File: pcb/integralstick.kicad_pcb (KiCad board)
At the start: 4 copper layers, 219 parts, among them J1 CONN_INTEGRALSTICK_FPGA_DEVICE, J2 CONN_INTEGRALSTICK_MCU_DEVICE, Q1 SSM6N58NU, Q2 SSM6N58NU, Q3 SSM6N58NU, U1 STM32F777NIH6‎, U10 DSC6083MI2A-032K768, U12 DSC6001HI2A-025.0000‎, U2 XC7A50T-1FTG256C, U3 S27KS0641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

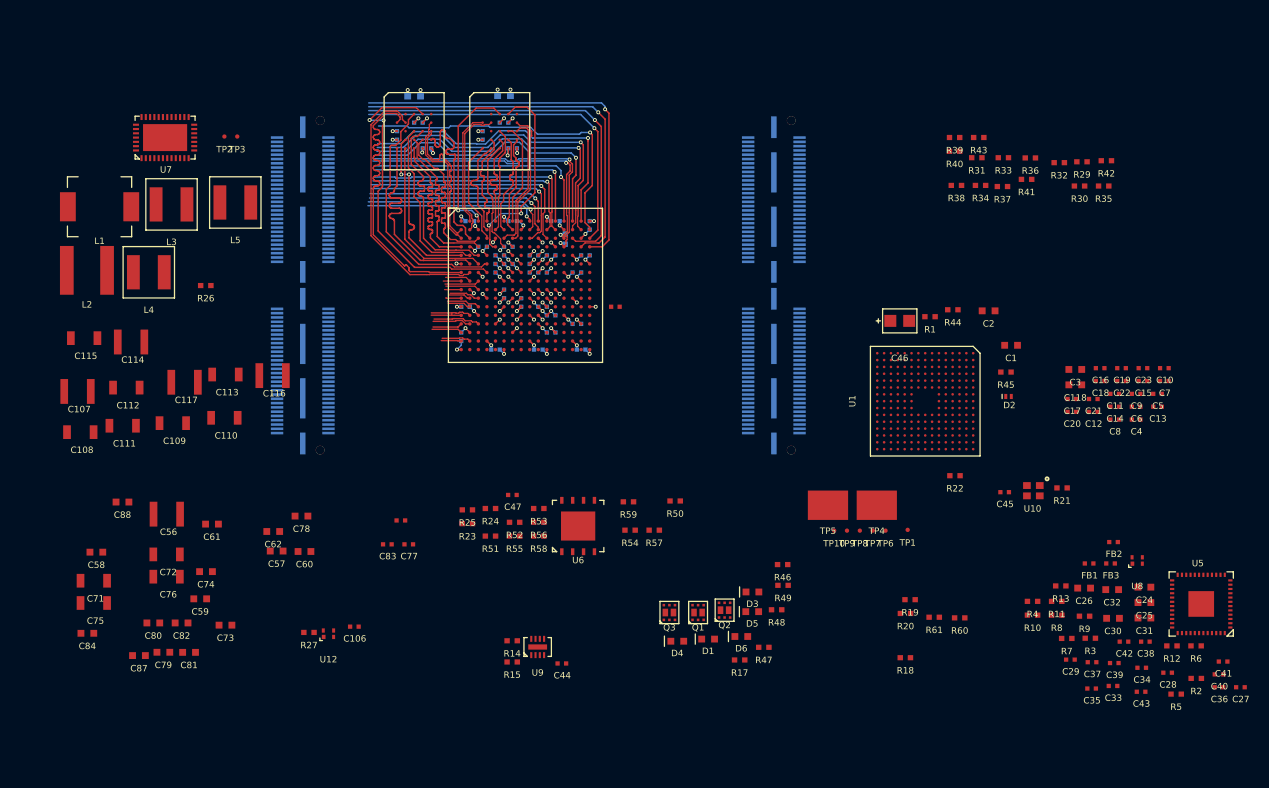
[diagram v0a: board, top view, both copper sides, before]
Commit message: Lots more routing of 3.3V GPIO bus
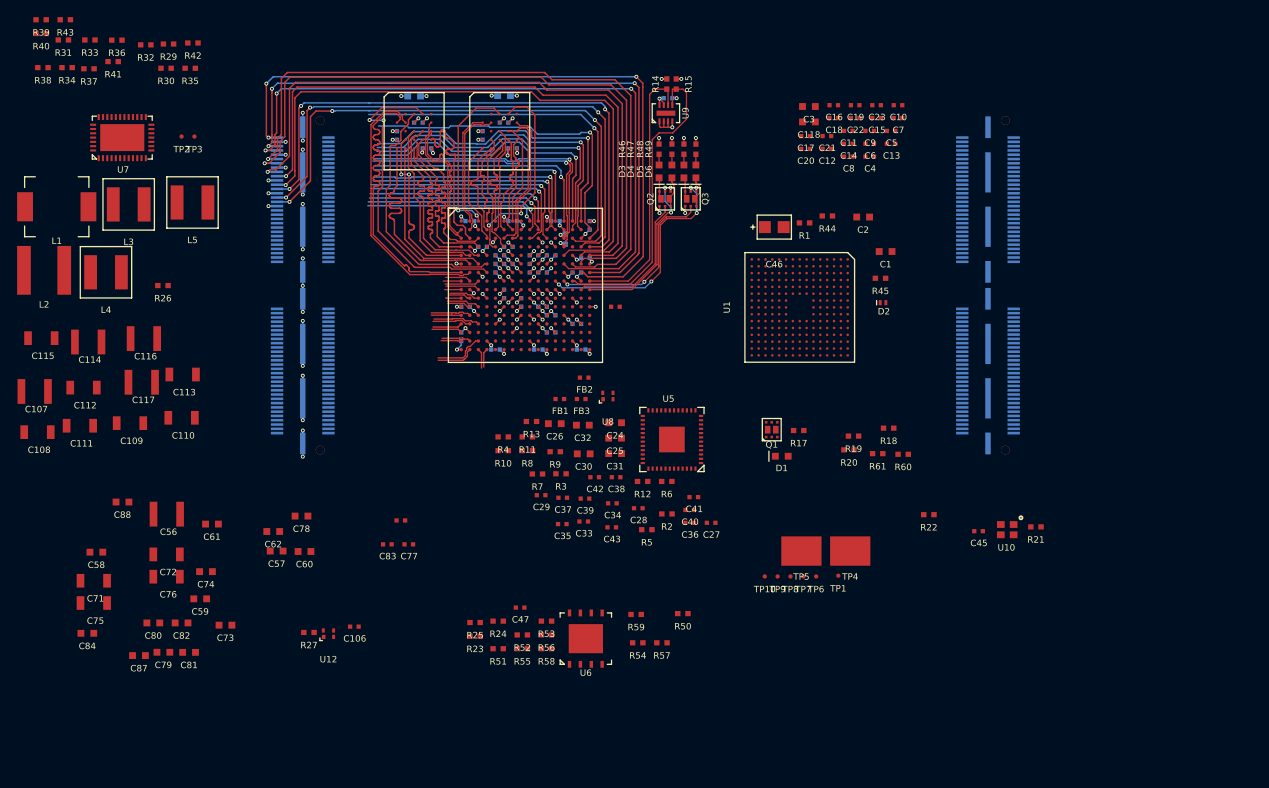
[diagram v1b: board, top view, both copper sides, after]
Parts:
- C44: moved to B.Cu
- moved R30 107.5 mm to (22.0, 17.7)
- moved R31 107.5 mm to (10.1, 14.3)
- moved R32 107.5 mm to (19.7, 14.9)
- moved R34 107.5 mm to (10.5, 17.6)
- moved R35 107.5 mm to (24.9, 17.7)
- moved R36 107.5 mm to (16.3, 14.4)
- moved R39 107.5 mm to (7.45, 12.0)
- moved R40 107.5 mm to (7.45, 13.6)
- moved R41 107.5 mm to (15.9, 16.9)
- moved R29 107.5 mm to (22.3, 14.8)
- moved R33 107.5 mm to (13.2, 14.3)
- moved R37 107.5 mm to (13.0, 17.7)
- moved R38 107.5 mm to (7.66, 17.6)
- moved R42 107.5 mm to (25.2, 14.7)
- moved R43 107.5 mm to (10.3, 12.0)
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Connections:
- U2 pad A12: /FPGA/IO_3V3_9 -> /FPGA/IO_3V3_22
- U2 pad A14: /FPGA/IO_3V3_25 -> /FPGA/IO_3V3_24
- U2 pad A15: /FPGA/IO_3V3_17 -> /FPGA/IO_3V3_12
- U2 pad B14: /FPGA/IO_3V3_15 -> /FPGA/IO_3V3_20
- U2 pad B16: /FPGA/IO_3V3_19 -> /FPGA/IO_3V3_28
- U2 pad C14: /FPGA/IO_3V3_22 -> /FPGA/IO_3V3_9
- U2 pad D11: /FPGA/IO_3V3_24 -> (no net)
- U2 pad D15: /FPGA/IO_3V3_26 -> /FPGA/IO_3V3_11
- U2 pad D16: /FPGA/IO_3V3_28 -> /FPGA/IO_3V3_13
- U2 pad D9: /FPGA/IO_3V3_11 -> /FPGA/IO_3V3_26
- U2 pad E13: /FPGA/IO_3V3_23 -> /FPGA/IO_3V3_15
- U2 pad E15: /FPGA/GPIO_LED0 -> /FPGA/IO_3V3_17
- U2 pad E16: /FPGA/IO_3V3_21 -> /FPGA/IO_3V3_19
- U2 pad F12: /FPGA/IO_3V3_27 -> (no net)
- U2 pad F13: (no net) -> /FPGA/IO_3V3_25
- U2 pad F14: (no net) -> /FPGA/IO_3V3_23
- U2 pad F15: /FPGA/IO_3V3_29 -> /FPGA/IO_3V3_21
- U2 pad G12: /FPGA/GPIO_LED2 -> (no net)
- U2 pad G15: /FPGA/I2C_SDA -> /FPGA/IO_3V3_29
- U2 pad G16: /FPGA/I2C_SCL -> /FPGA/IO_3V3_27
- U2 pad H11: /FPGA/GPIO_LED1 -> (no net)
- U2 pad H13: (no net) -> /FPGA/GPIO_LED2
- U2 pad H14: (no net) -> /FPGA/I2C_SDA
- U2 pad H16: /FPGA/IO_3V3_20 -> /FPGA/I2C_SCL
- U2 pad J15: /FPGA/IO_3V3_12 -> /FPGA/GPIO_LED0
- U2 pad J16: /FPGA/IO_3V3_13 -> /FPGA/GPIO_LED1
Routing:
- net /GND: track 51.8 -> 319.4 mm, vias 47 -> 68
- net /3V3: track 15.2 -> 153.3 mm, vias 15 -> 28
- net /FPGA/IO_3V3_29: track 0.00 -> 80.7 mm, vias 0 -> 3
- net /FPGA/IO_3V3_23: track 0.00 -> 79.0 mm, vias 0 -> 1
- net /FPGA/IO_3V3_27: track 0.00 -> 77.3 mm, vias 0 -> 3
- net /FPGA/IO_3V3_21: track 0.00 -> 76.9 mm, vias 0 -> 1
- net /1V8: track 21.8 -> 98.4 mm
- net /FPGA/IO_3V3_13: track 0.00 -> 65.9 mm, vias 0 -> 3
- net /FPGA/IO_3V3_11: track 0.00 -> 64.8 mm, vias 0 -> 3
- net /FPGA/IO_3V3_25: track 33.4 -> 79.1 mm, vias 1 -> 3
- net /FPGA/IO_3V3_26: track 45.2 -> 0.00 mm, vias 1 -> 0
- net /FPGA/IO_3V3_9: track 26.8 -> 64.1 mm, vias 1 -> 3
- net /FPGA/IO_3V3_12: track 0.00 -> 36.9 mm, vias 0 -> 1
- net /FPGA/I2C_SDA: track 0.00 -> 36.5 mm
- net /FPGA/IO_3V3_15: track 35.8 -> 71.8 mm
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
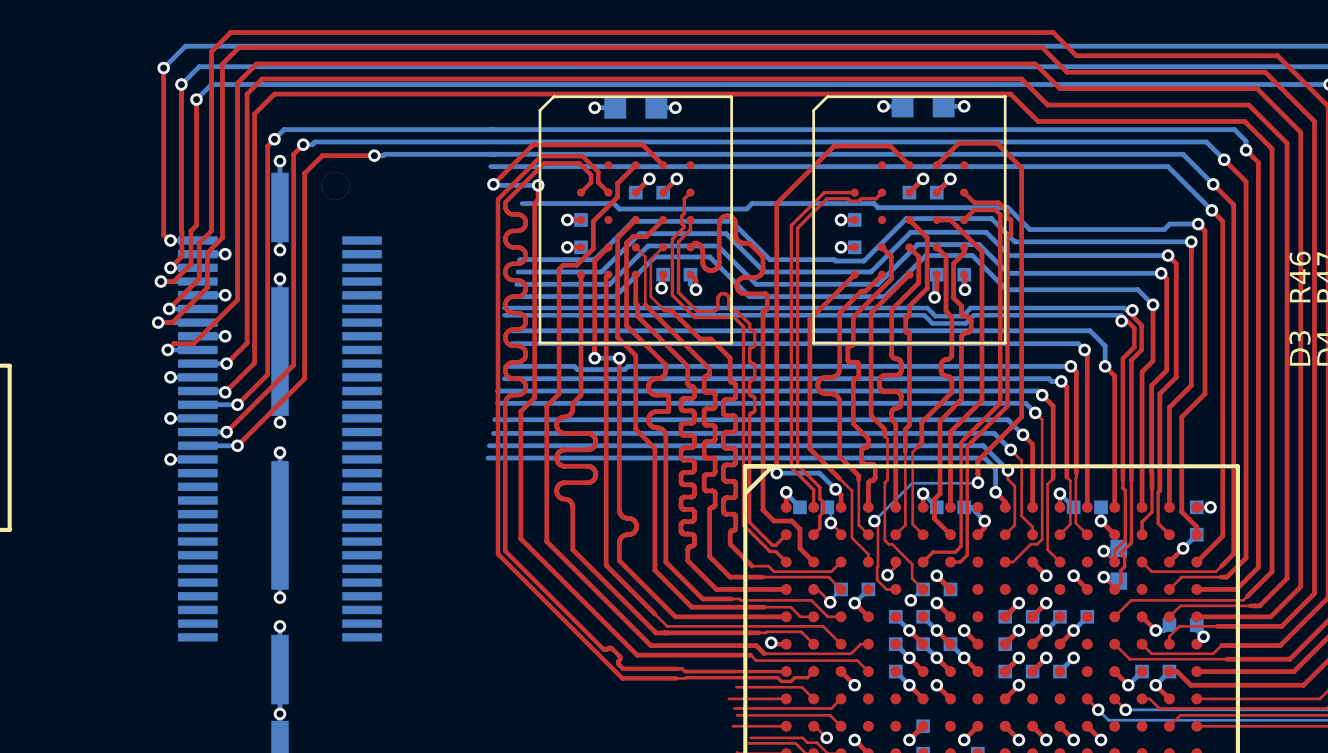
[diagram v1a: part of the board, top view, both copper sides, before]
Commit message: Continued routing 3.3V GPIO bus. Everything that can be fanned out on top metal is done.
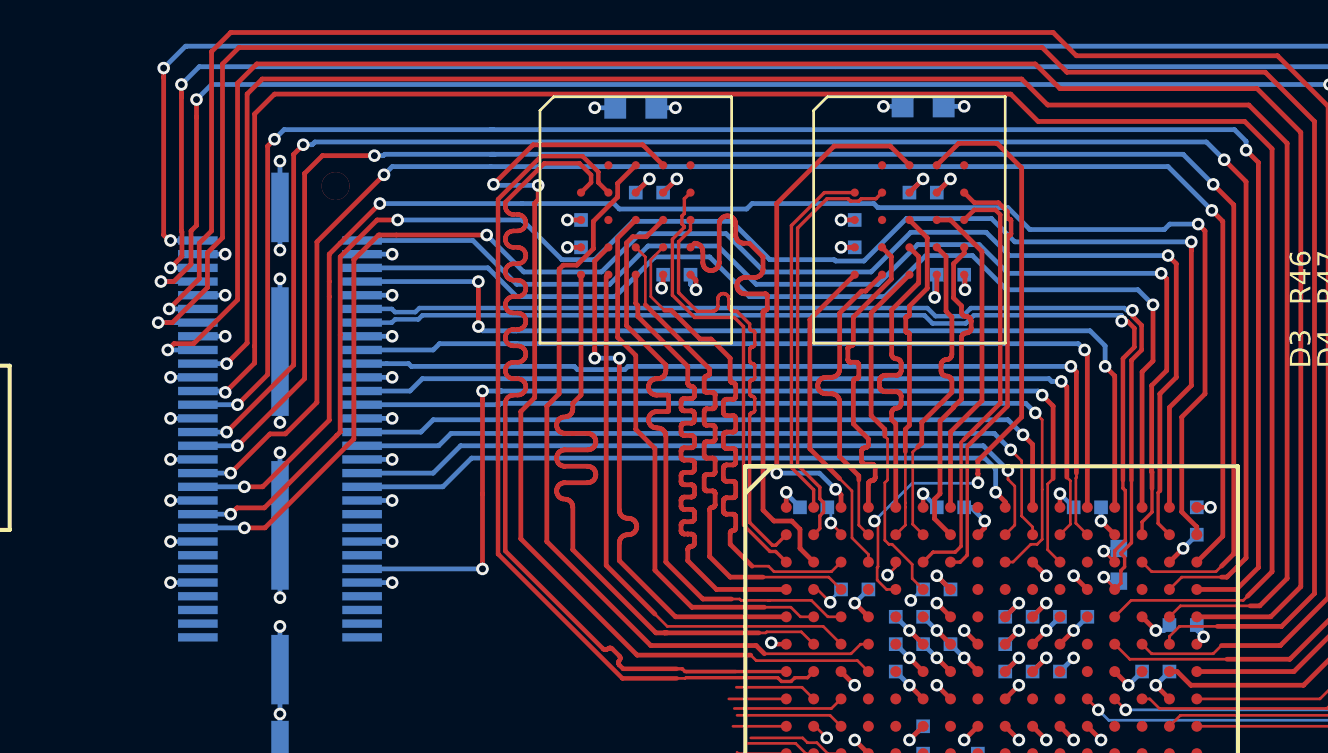
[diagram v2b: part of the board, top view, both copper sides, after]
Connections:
- J1 pad 101: /FPGA/IO_3V3_16 -> /FPGA/IO_3V3_18
- J1 pad 102: /FPGA/IO_3V3_17 -> /FPGA/IO_3V3_19
- J1 pad 103: /FPGA/IO_3V3_18 -> /FPGA/IO_3V3_20
- J1 pad 104: /FPGA/IO_3V3_19 -> /FPGA/IO_3V3_21
- J1 pad 107: /FPGA/IO_3V3_20 -> /FPGA/IN_3V3_0_N
- J1 pad 108: /FPGA/IO_3V3_21 -> /FPGA/IO_3V3_22
- J1 pad 109: /FPGA/IO_3V3_22 -> /FPGA/IN_3V3_0_P
- J1 pad 78: /FPGA/IN_3V3_0_P -> /FPGA/IO_3V3_3
- J1 pad 79: /FPGA/IO_3V3_3 -> /FPGA/IO_3V3_4
- J1 pad 80: /FPGA/IN_3V3_0_N -> /FPGA/IO_3V3_5
- J1 pad 83: /FPGA/IO_3V3_4 -> /FPGA/IO_3V3_6
- J1 pad 84: /FPGA/IO_3V3_5 -> /FPGA/IO_3V3_7
- J1 pad 85: /FPGA/IO_3V3_6 -> /FPGA/IO_3V3_8
- J1 pad 86: /FPGA/IO_3V3_7 -> /FPGA/IO_3V3_9
- J1 pad 89: /FPGA/IO_3V3_8 -> /FPGA/IO_3V3_10
- J1 pad 90: /FPGA/IO_3V3_9 -> /FPGA/IO_3V3_11
- J1 pad 91: /FPGA/IO_3V3_10 -> /FPGA/IO_3V3_12
- J1 pad 92: /FPGA/IO_3V3_11 -> /FPGA/IO_3V3_13
- J1 pad 95: /FPGA/IO_3V3_12 -> /FPGA/IO_3V3_14
- J1 pad 96: /FPGA/IO_3V3_13 -> /FPGA/IO_3V3_15
- J1 pad 97: /FPGA/IO_3V3_14 -> /FPGA/IO_3V3_16
- J1 pad 98: /FPGA/IO_3V3_15 -> /FPGA/IO_3V3_17
- U2 pad A10: /FPGA/IO_3V3_5 -> /FPGA/IO_3V3_12
- U2 pad A12: /FPGA/IO_3V3_22 -> /FPGA/IO_3V3_20
- U2 pad A13: /FPGA/IO_3V3_14 -> /FPGA/IO_3V3_24
- U2 pad A14: /FPGA/IO_3V3_24 -> /FPGA/IO_3V3_26
- U2 pad A15: /FPGA/IO_3V3_12 -> /FPGA/IO_3V3_5
- U2 pad A9: /FPGA/IO_3V3_3 -> /FPGA/IO_3V3_6
- U2 pad B10: /FPGA/IO_3V3_6 -> /FPGA/IO_3V3_10
- U2 pad B11: /FPGA/IO_3V3_7 -> /FPGA/IO_3V3_16
- U2 pad B12: /FPGA/IO_3V3_8 -> /FPGA/IO_3V3_18
- U2 pad B14: /FPGA/IO_3V3_20 -> /FPGA/IO_3V3_28
- U2 pad B15: /FPGA/IO_3V3_16 -> /FPGA/IO_3V3_3
- U2 pad B16: /FPGA/IO_3V3_28 -> /FPGA/IO_3V3_7
- U2 pad B9: /FPGA/IO_3V3_4 -> /FPGA/IO_3V3_8
- U2 pad C14: /FPGA/IO_3V3_9 -> /FPGA/IO_3V3_11
- U2 pad C16: /FPGA/IO_3V3_18 -> /FPGA/IO_3V3_9
- U2 pad C9: /FPGA/IO_3V3_1 -> /FPGA/IO_3V3_14
- U2 pad D15: /FPGA/IO_3V3_11 -> /FPGA/IO_3V3_13
- U2 pad D16: /FPGA/IO_3V3_13 -> /FPGA/IO_3V3_15
- U2 pad D8: /FPGA/IO_3V3_10 -> /FPGA/IO_3V3_4
- U2 pad D9: /FPGA/IO_3V3_26 -> /FPGA/IO_3V3_1
- U2 pad E13: /FPGA/IO_3V3_15 -> /FPGA/IO_3V3_17
- U2 pad E15: /FPGA/IO_3V3_17 -> /FPGA/IO_3V3_19
- U2 pad E16: /FPGA/IO_3V3_19 -> /FPGA/IO_3V3_21
- U2 pad F15: /FPGA/IO_3V3_21 -> /FPGA/IO_3V3_22
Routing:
- net /FPGA/IO_3V3_22: track 26.8 -> 76.9 mm
- net /FPGA/IO_3V3_26: track 0.00 -> 39.5 mm, vias 0 -> 1
- net /FPGA/IO_3V3_3: track 20.3 -> 57.2 mm, vias 1 -> 3
- net /FPGA/IO_3V3_5: track 22.3 -> 57.5 mm, vias 1 -> 3
- net /3V3: track 153.3 -> 188.4 mm, vias 28 -> 40
- net /FPGA/IO_3V3_7: track 26.3 -> 57.1 mm, vias 1 -> 3
- net /FPGA/IO_3V3_10: track 0.00 -> 27.6 mm, vias 0 -> 1
- net /FPGA/IO_3V3_1: track 26.2 -> 0.00 mm, vias 1 -> 0
- net /FPGA/IO_3V3_4: track 21.9 -> 0.00 mm, vias 1 -> 0
- net /FPGA/CLK_3V3_0: track 26.5 -> 38.1 mm, vias 1 -> 3
- net /FPGA/IO_3V3_12: track 36.9 -> 27.4 mm
- net /FPGA/IO_3V3_18: track 40.4 -> 32.5 mm
- net /FPGA/IO_3V3_15: track 71.8 -> 65.9 mm, vias 1 -> 3
- net /FPGA/IN_3V3_0_N: track 33.7 -> 39.0 mm
- net /FPGA/IN_3V3_0_P: track 35.3 -> 40.6 mm
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
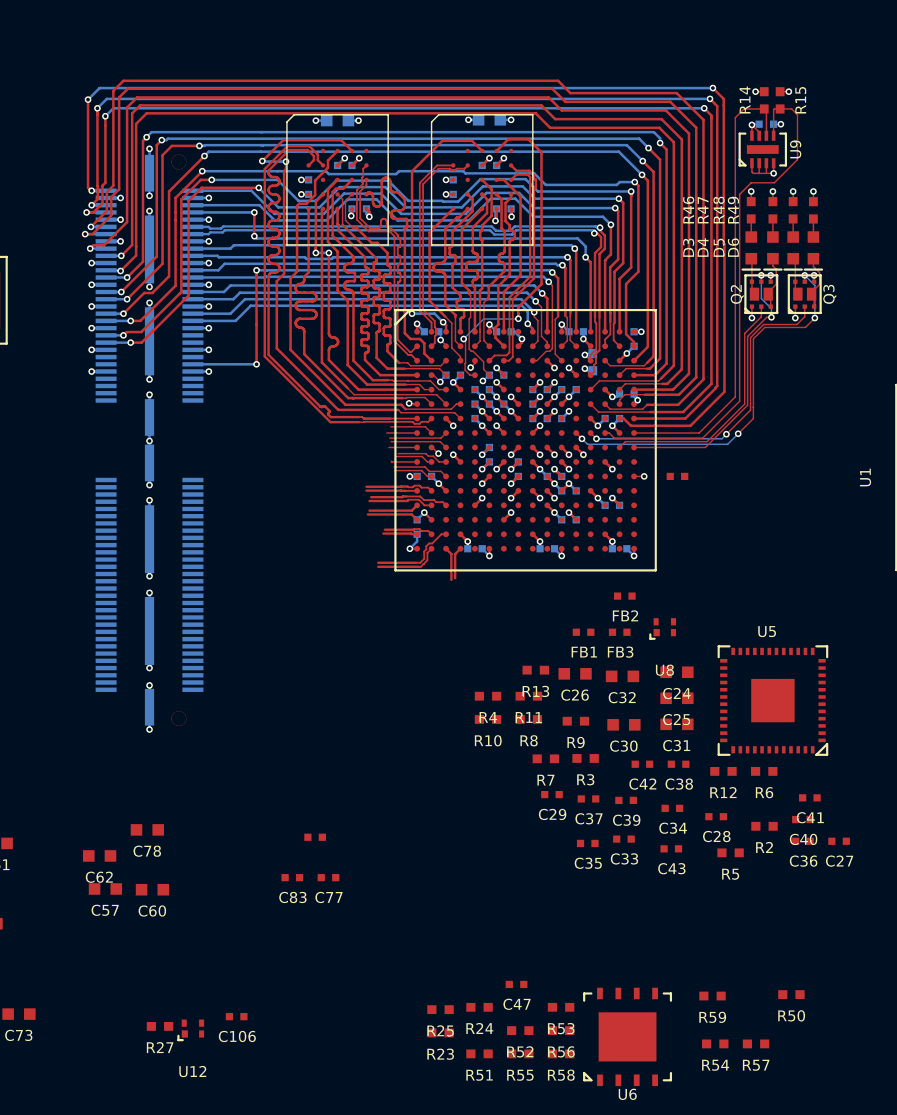
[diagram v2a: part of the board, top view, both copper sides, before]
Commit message: Finished routing 3.3V GPIO bus
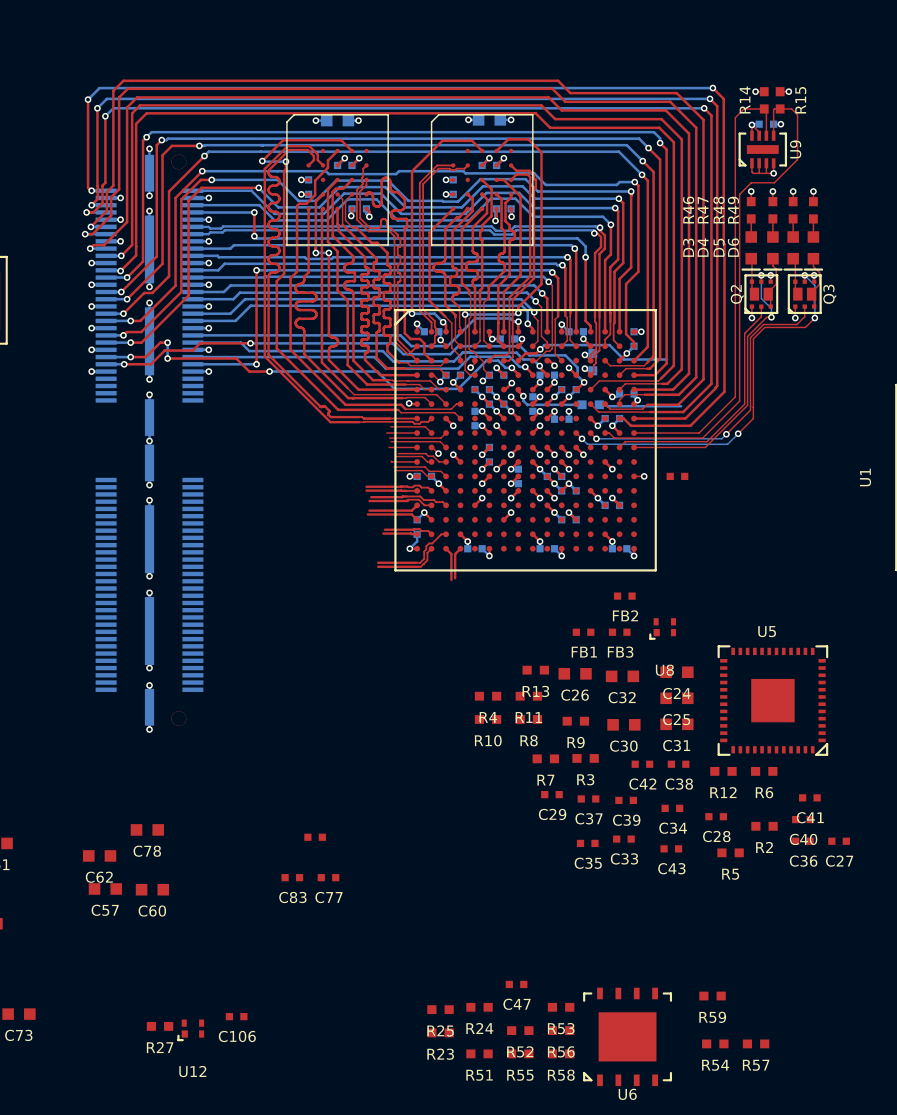
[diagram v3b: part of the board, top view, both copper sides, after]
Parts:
- R50: moved to B.Cu
- moved R50 43.1 mm to (68.5, 40.5)
- moved C68 1.12 mm to (65.5, 38.5)
- moved C105 0.56 mm to (62.8, 36.0)
- moved C89 0.50 mm to (66.5, 41.5)
- moved C64 0.50 mm to (60.5, 41.5)
- moved C69 0.50 mm to (63.5, 45.5)
- moved C70 0.50 mm to (64.5, 40.5)
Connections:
- U2 pad A8: /FPGA/IO_3V3_2 -> /FPGA/IO_3V3_4
- U2 pad D10: /FPGA/IO_3V3_0 -> /FPGA/IO_3V3_2
- U2 pad D8: /FPGA/IO_3V3_4 -> /FPGA/IO_3V3_1
- U2 pad D9: /FPGA/IO_3V3_1 -> /FPGA/IO_3V3_0
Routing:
- net /FPGA/CLK_3V3_1: track 0.00 -> 36.3 mm, vias 0 -> 3
- net /FPGA/IO_3V3_1: track 0.00 -> 32.1 mm, vias 0 -> 5
- net /FPGA/IO_3V3_2: track 0.00 -> 26.8 mm, vias 0 -> 1
- net /FPGA/IO_3V3_0: track 0.00 -> 24.7 mm, vias 0 -> 1
- net /FPGA/IO_3V3_4: track 0.00 -> 24.4 mm, vias 0 -> 1
- net /PSU_TEMP: track 0.00 -> 11.1 mm, vias 0 -> 1
- net /QSPI_CLK: track 0.00 -> 5.69 mm
- net Net-(R50-Pad1): track 0.00 -> 5.10 mm, vias 0 -> 1
- net /GND: track 319.4 -> 317.9 mm
- net /1V0: track 30.9 -> 30.1 mm
- net /RAM/RAM0_RST_N: track 23.4 -> 24.0 mm
